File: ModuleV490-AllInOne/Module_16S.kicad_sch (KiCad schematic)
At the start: 59 parts, among them J14 BALANCE BOARD, J15 BALANCE BOARD, J6 CELL CONNECTOR PLUG, J7 CELL CONNECTOR, U1 MAX14921ECS+T, U2 MCP1501-40xSN, U3 MCP33151-05-E/MS, U6 MCP1502T-45E/CHY

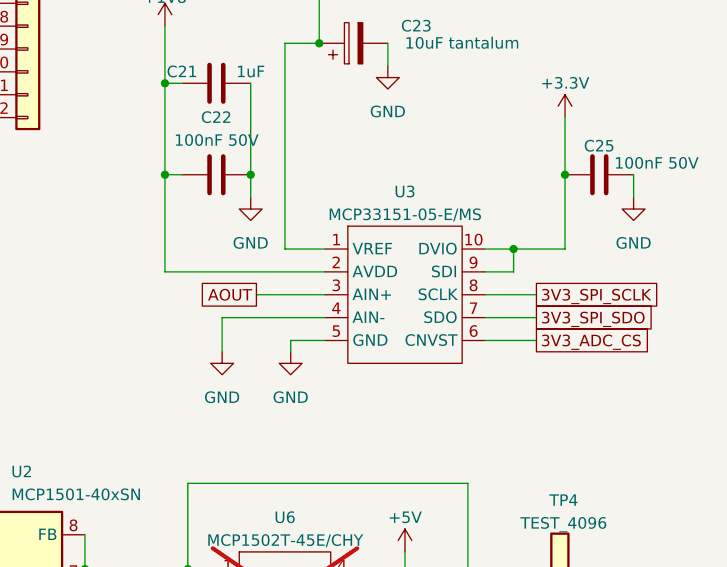
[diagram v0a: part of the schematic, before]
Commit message: Removed MCP33131 symbol and cloned to MCP33151
No physical change to circuit or board, just ensuring BOM looks correct
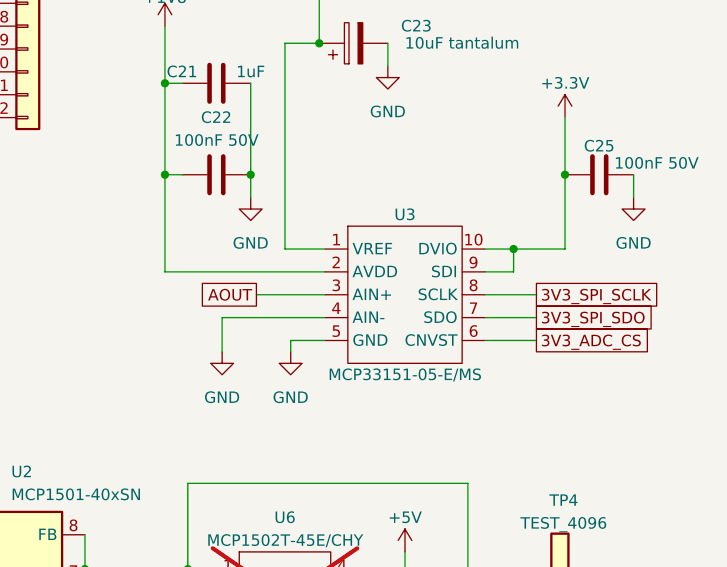
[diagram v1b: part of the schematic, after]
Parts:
- U3: symbol MicroChip:MCP33131-05-E/MS -> mcp33151:MCP33151-05-E/MS
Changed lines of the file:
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@@
     )
   )
-  (symbol (lib_id "MicroChip:MCP33131-05-E/MS") (at 250.19 93.345 0) (unit 1)
+  (symbol (lib_id "mcp33151:MCP33151-05-E/MS") (at 250.19 93.345 0) (unit 1)
     (in_bom yes) (on_board yes) (dnp no) (fields_autoplaced)
-    (property "Reference" "U3" (at 250.19 81.915 0)
+    (property "Reference" "U3" (at 250.19 84.455 0)
       (effects (font (size 1.27 1.27)))
     )
-    (property "Value" "MCP33151-05-E/MS" (at 250.19 84.455 0)
+    (property "Value" "MCP33151-05-E/MS" (at 250.19 102.235 0)
       (effects (font (size 1.27 1.27)))
     )
@@
       (effects (font (size 1.27 1.27)) hide)
     )
-    (property "Datasheet" "https://ww1.microchip.com/downloads/aemDocuments/documents/APID/ProductDocuments/DataSheets/MCP33151-XX-Family-Data-Sheet-DS20006220A.pdf" (at 241.3 80.645 0)
+    (property "Datasheet" "https://www.microchip.com/en-us/product/mcp33151-05" (at 241.3 80.645 0)
+      (effects (font (size 1.27 1.27)) hide)
+    )
+    (property "LCSCStockCode" "C635984" (at 250.19 93.345 0)
       (effects (font (size 1.27 1.27)) hide)
     )
@@
       (effects (font (size 1.27 1.27)) hide)
     )
-    (property "LCSCStockCode" "C635984" (at 250.19 93.345 0)
-      (effects (font (size 1.27 1.27)) hide)
-    )

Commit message: Update Module_16S.kicad_sch
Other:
- note added: "Getting the Most Out of the MAX14920/MAX14921 High-Accuracy Battery-Measurement AFEs"
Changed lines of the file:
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@@
     (effects (font (size 1.27 1.27)) (justify right bottom))
+  )
+  (text "Getting the Most Out of the MAX14920/MAX14921 High-Accuracy Battery-Measurement AFEs"
+    (at 96.52 157.48 0)
+    (effects (font (size 1.27 1.27)) (justify left bottom) (href "https://pdfserv.maximintegrated.com/en/an/AN5760.pdf"))
   )
   (text "Eval Board" (at 18.415 34.925 0)

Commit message: Squashed commit of the following:
commit 382df4b7a104fb34cc4a4da3f786b21ade19fcd5
Author: GitHub Action <action@github.com>
Date:   Fri Apr 18 11:47:05 2025 +0000

    CI: pcb-artifacts-ModuleV490-AllInOne

commit b35cb7a0d3894cf57b33edb037eb829bc9ec5ea4
Author: Stuart Pittaway <1201909+stuartpittaway@users.noreply.github.com>
Date:   Fri Apr 18 12:44:57 2025 +0100

    Minor tweaks

commit ea046b7e5d836263693da1b47c6dfb3dc918925c
Author: Stuart Pittaway <1201909+stuartpittaway@users.noreply.github.com>
Date:   Fri Apr 18 12:44:16 2025 +0100

    PCB Panel of Temp sensors

commit ba929f4700586b6858203bc466c6b18e911d661e
Author: GitHub Action <action@github.com>
Date:   Sun Mar 23 15:29:50 2025 +0000

    CI: pcb-artifacts-ModuleV490-AllInOne

commit 1dbbac7378fdc5acb48c43d3f728917ce2318f16
Author: GitHub Action <action@github.com>
Date:   Wed Apr 10 09:57:21 2024 +0000

    CI: pcb-artifacts-ModuleV490-AllInOne

commit 35f617d42fc7a6a7ab395d232005d3307c26595c
Author: Stuart Pittaway <1201909+stuartpittaway@users.noreply.github.com>
Date:   Wed Apr 10 10:55:49 2024 +0100

    Update pcb-artifacts-modulev490-allinone.yaml

commit c8295c0089ea2c5e86742be6a5572142963deb8f
Author: Stuart Pittaway <1201909+stuartpittaway@users.noreply.github.com>
Date:   Wed Apr 10 10:53:50 2024 +0100

    Update pcb-artifacts-modulev490-allinone.yaml

commit d19b2989a6afd4cac4ecf3c8c78554eedba7b99a
Author: Stuart Pittaway <1201909+stuartpittaway@users.noreply.github.com>
Date:   Wed Apr 10 10:50:28 2024 +0100

    Update pcb-artifacts-modulev490-allinone.yaml

commit 8478886fe70d1ee53aca3bbd908099e6f38ff11d
Author: Stuart Pittaway <1201909+stuartpittaway@users.noreply.github.com>
Date:   Wed Apr 10 10:41:28 2024 +0100

    Update pcb-artifacts-modulev490-allinone.yaml

commit afeafa74721a9b51459c6106f0a15ae423229204
Author: Stuart Pittaway <1201909+stuartpittaway@users.noreply.github.com>
Date:   Wed Apr 10 10:39:10 2024 +0100

    Inductor part change - fix workflows

commit 70fd25ba43b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
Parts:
- removed JP2: LDO_EN, Jumper:SolderJumper-3_P1.3mm_Bridged12_RoundedPad1.0x1.5mm_NumberLabels, symbol Jumper:SolderJumper_3_Bridged12
- removed U2: MCP1501-40xSN, Package_SO:SOIC-8_3.9x4.9mm_P1.27mm, symbol Reference_Voltage:MCP1501-40xSN
- added FID1, FID2, FID3, FID4: Fiducial, Fiducial:Fiducial_1.5mm_Mask3mm, symbol Mechanical:Fiducial
- J6: value CELL CONNECTOR PLUG -> MALE PLUG; LCSCStockCode C489973 -> C430370; PartNumber WJ15EDGK-3.81-17P -> DB2EK-3.81-17P-GN-S; now left out of the parts list
- J7: LCSCStockCode C489980 -> C430372; PartNumber WJ15EDGRC-3.81-17P -> DB2ERC-3.81-17P-GN
- TP4: value TEST_4096 -> TEST_VREF
- U6: LCSCStockCode (none) -> C5236158; now fitted; now in the parts list
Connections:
- net LDOIN is gone; now on net +5V: U1.13 (LDOIN)
- net VREF4096 renamed VREF
